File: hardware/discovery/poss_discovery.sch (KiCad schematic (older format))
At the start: 28 parts, among them SW1 SW_PUSH, SW10 SW_PUSH, SW11 SW_PUSH, SW12 SW_PUSH, SW13 SW_PUSH, SW14 SW_PUSH, SW15 SW_PUSH, SW16 SW_PUSH, SW17 SW_PUSH, SW18 SW_PUSH, SW19 SW_PUSH, SW2 SW_PUSH, SW20 SW_PUSH, SW21 SW_PUSH, SW22 SW_PUSH, SW3 SW_PUSH, SW4 SW_PUSH, SW5 SW_PUSH, SW6 SW_PUSH, SW7 SW_PUSH, SW8 SW_PUSH, SW9 SW_PUSH, U1 STM32F4_DISCO_Header

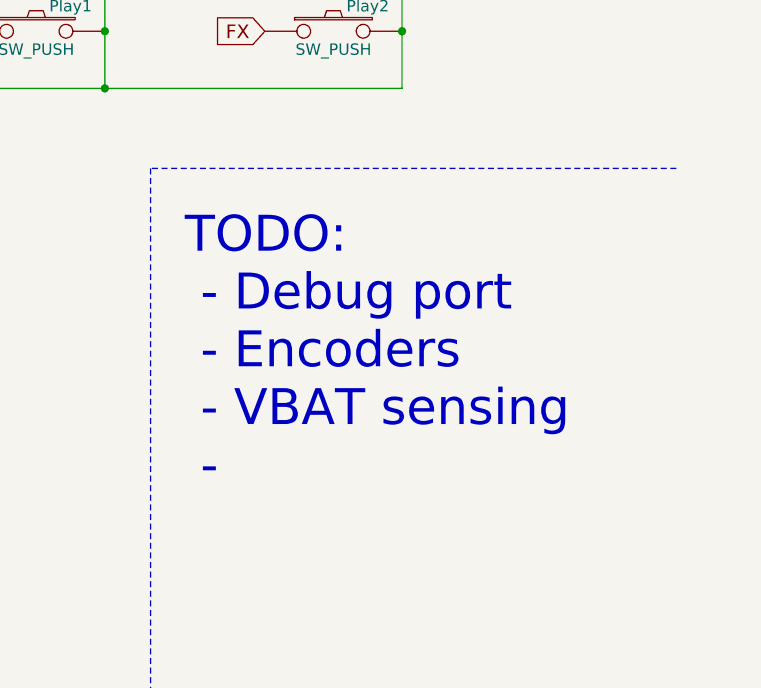
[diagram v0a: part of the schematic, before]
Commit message: Discovery: add crystal
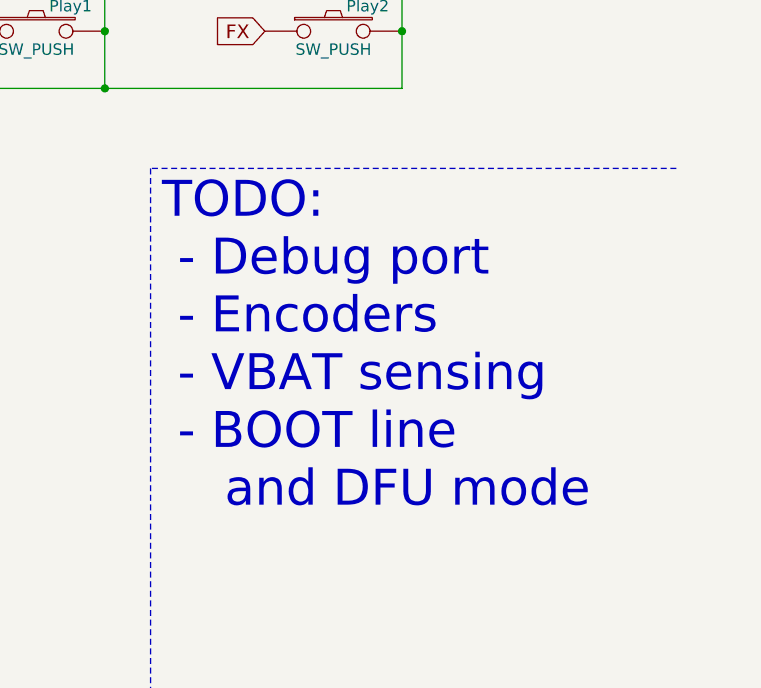
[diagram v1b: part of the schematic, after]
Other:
- note added: "TODO:\n - Debug port\n - Encoders\n - VBAT sensing\n - BOOT line \n and DFU mode"
- note removed: "TODO:\n - Debug port\n - Encoders\n - VBAT sensing\n -"
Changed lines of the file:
@@
 F1 "audio.sch" 60
 $EndSheet
-Text Notes 9000 5500 0    157  ~ 0
-TODO:\n - Debug port\n - Encoders\n - VBAT sensing\n -
+Text Notes 8900 5600 0    157  ~ 0
+TODO:\n - Debug port\n - Encoders\n - VBAT sensing\n - BOOT line \n    and DFU mode
 Wire Wire Line
 	7400 750  7400 3750

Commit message: Discovery: STM32F4 power a filtering
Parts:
- removed RV1, RV2: POT, Potentiometers:Potentiometer_WirePads_Small, symbol POT-RESCUE-poss_discovery
- added U6, U7: encoder_and_switch, symbol encoder_and_switch
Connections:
- net labels added: ENC_1_A, ENC_1_B, ENC_1_SW, ENC_2_A, ENC_2_B, ENC_2_SW
- wire segments 14 -> 6
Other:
- note added: "TODO:\n - Debug port\n - Encoders\n - VBAT sensing\n - BOOT line \n and DFU mode\n - NReset pull-up"
- note removed: "TODO:\n - Debug port\n - Encoders\n - VBAT sensing\n - BOOT line \n and DFU mode"
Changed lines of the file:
@@
-$EndComp
-$Comp
-L POT-RESCUE-poss_discovery RV2
-U 1 1 583F8AB3
-P 4700 5900
-F 0 "RV2" H 4700 5820 50  0000 C CNN
-F 1 "POT" H 4700 5900 50  0000 C CNN
-F 2 "Potentiometers:Potentiometer_WirePads_Small" H 4700 5900 50  0001 C CNN
-F 3 "" H 4700 5900 50  0000 C CNN
-	1    4700 5900
-	1    0    0    -1
-$EndComp
-$Comp
-L POT-RESCUE-poss_discovery RV1
-U 1 1 583FAB8F
-P 3350 5900
-F 0 "RV1" H 3350 5820 50  0000 C CNN
-F 1 "POT" H 3350 5900 50  0000 C CNN
-F 2 "Potentiometers:Potentiometer_WirePads_Small" H 3350 5900 50  0001 C CNN
-F 3 "" H 3350 5900 50  0000 C CNN
-	1    3350 5900
-	1    0    0    -1
 $EndComp
 $Comp
@@
 Text GLabel 4400 1650 0    60   Input ~ 0
 3V3
-Text GLabel 3350 5650 2    60   Input ~ 0
-POT1
-Text GLabel 4700 5650 2    60   Input ~ 0
-POT2
-Text GLabel 3100 5900 0    60   Input ~ 0
-3V3
-Text GLabel 4450 5900 0    60   Input ~ 0
-3V3
 Text GLabel 2200 1350 2    60   Input ~ 0
 GND
@@
 F1 "power.sch" 60
 $EndSheet
+Text GLabel 5500 4950 2    60   Input ~ 0
+GND
 $Comp
 L GND #PWR01
-U 1 1 585DAFE1
-P 4950 6000
-F 0 "#PWR01" H 4950 6000 30  0001 C CNN
-F 1 "GND" H 4950 5930 30  0001 C CNN
-F 2 "" H 4950 6000 60  0001 C CNN
-F 3 "" H 4950 6000 60  0001 C CNN
-	1    4950 6000
-	1    0    0    -1
-$EndComp
-$Comp
-L GND #PWR02
-U 1 1 585DB05F
-P 3600 6000
-F 0 "#PWR02" H 3600 6000 30  0001 C CNN
-F 1 "GND" H 3600 5930 30  0001 C CNN
-F 2 "" H 3600 6000 60  0001 C CNN
-F 3 "" H 3600 6000 60  0001 C CNN
-	1    3600 6000
-	1    0    0    -1
-$EndComp
-Text GLabel 5500 4950 2    60   Input ~ 0
-GND
-$Comp
-L GND #PWR03
 U 1 1 585DBA46
 P 5500 5100
-F 0 "#PWR03" H 5500 5100 30  0001 C CNN
+F 0 "#PWR01" H 5500 5100 30  0001 C CNN
 F 1 "GND" H 5500 5030 30  0001 C CNN
 F 2 "" H 5500 5100 60  0001 C CNN
@@
 F1 "audio.sch" 60
 $EndSheet
-Text Notes 8900 5600 0    157  ~ 0
-TODO:\n - Debug port\n - Encoders\n - VBAT sensing\n - BOOT line \n    and DFU mode
+Text Notes 8950 5850 0    157  ~ 0
+TODO:\n - Debug port\n - Encoders\n - VBAT sensing\n - BOOT line \n    and DFU mode\n - NReset pull-up
 Wire Wire Line
 	7400 750  7400 3750
@@
 Connection ~ 9950 1800
 Connection ~ 9950 1450
-Wire Wire Line
-	4850 5900 4950 5900
-Wire Wire Line
-	4700 5750 4700 5650
-Wire Wire Line
-	4550 5900 4450 5900
-Wire Wire Line
-	3500 5900 3600 5900
-Wire Wire Line
-	3350 5750 3350 5650
-Wire Wire Line
-	3200 5900 3100 5900
 Connection ~ 9950 3500
 Connection ~ 8650 3500
 Connection ~ 7400 3500
-Wire Wire Line
-	3600 5900 3600 6000
-Wire Wire Line
-	4950 5900 4950 6000
 Wire Wire Line
 	5350 4950 5500 4950
@@
 Text GLabel 6800 3750 0    60   Input ~ 0
 WAKEUP
+$Comp
+L encoder_and_switch U6
+U 1 1 585F9C7A
+P 1750 5250
+F 0 "U6" H 1500 5050 60  0000 C CNN
+F 1 "encoder_and_switch" H 2100 5100 60  0000 C CNN
+F 2 "" H 1750 5250 60  0001 C CNN
+F 3 "" H 1750 5250 60  0001 C CNN
+	1    1750 5250
+	1    0    0    -1
+$EndComp
+$Comp
+L encoder_and_switch U7
+U 1 1 585FA833
+P 3750 5250
+F 0 "U7" H 3500 5050 60  0000 C CNN
+F 1 "encoder_and_switch" H 4100 5100 60  0000 C CNN
+F 2 "" H 3750 5250 60  0001 C CNN
+F 3 "" H 3750 5250 60  0001 C CNN
+	1    3750 5250
+	1    0    0    -1
+$EndComp
+Text GLabel 2150 5600 2    60   Input ~ 0
+WAKEUP
+Text GLabel 4150 5600 2    60   Input ~ 0
+WAKEUP
+Text GLabel 1350 5600 0    60   Input ~ 0
+ENC_1_SW
+Text GLabel 3350 5600 0    60   Input ~ 0
+ENC_2_SW
+Text GLabel 1500 5950 3    60   Input ~ 0
+ENC_1_A
+Text GLabel 1750 5950 3    60   Input ~ 0
+WAKEUP
+Text GLabel 2000 5950 3    60   Input ~ 0
+ENC_1_B
+Text GLabel 3500 5950 3    60   Input ~ 0
+ENC_2_A
+Text GLabel 3750 5950 3    60   Input ~ 0
+WAKEUP
+Text GLabel 4000 5950 3    60   Input ~ 0
+ENC_2_B
 $EndSCHEMATC

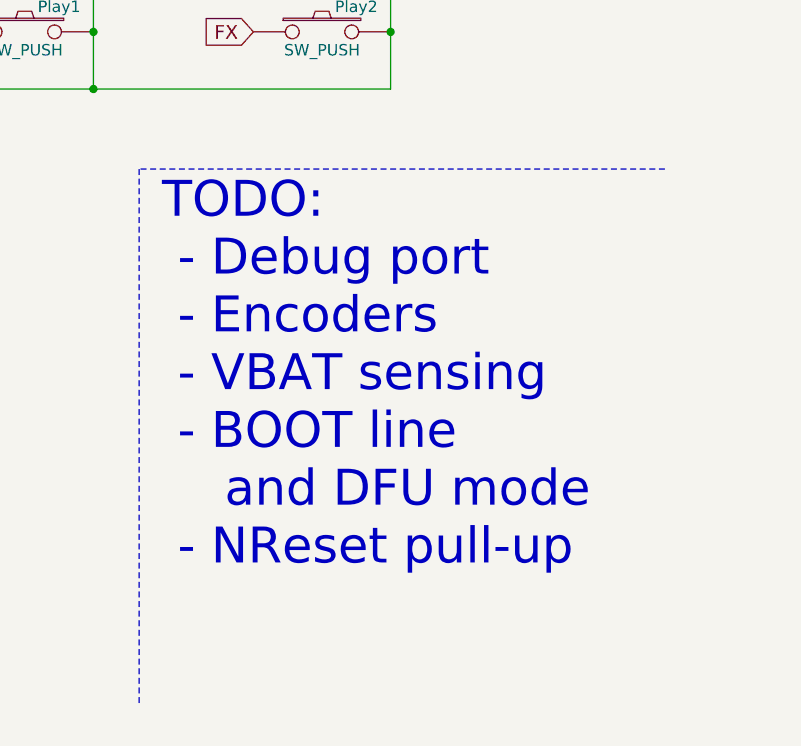
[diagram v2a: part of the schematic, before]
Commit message: Discovery: Start routing LEDs and buttons
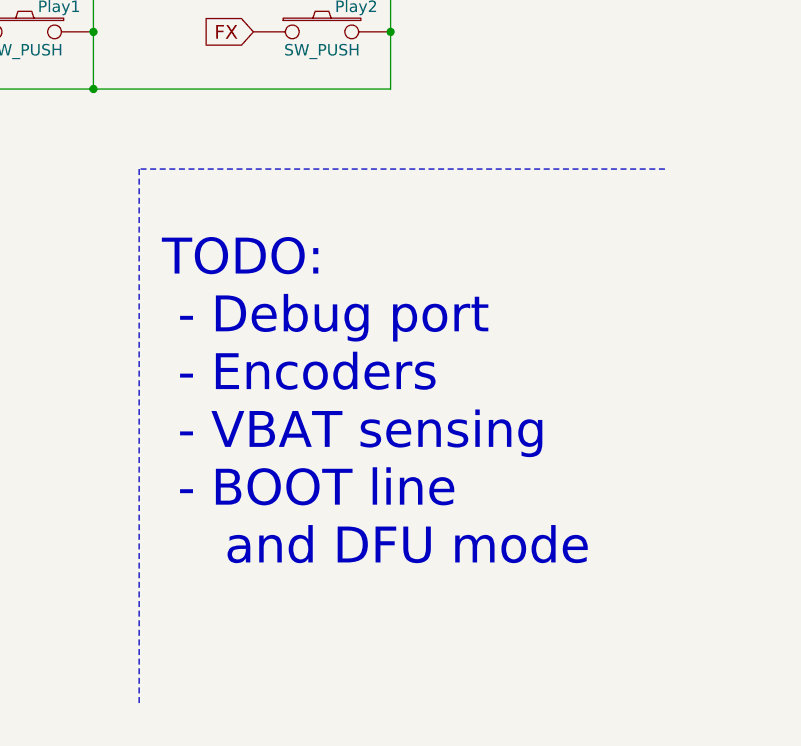
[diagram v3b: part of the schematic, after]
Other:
- note added: "TODO:\n - Debug port\n - Encoders\n - VBAT sensing\n - BOOT line \n and DFU mode"
- note removed: "TODO:\n - Debug port\n - Encoders\n - VBAT sensing\n - BOOT line \n and DFU mode\n - NReset pull-up"
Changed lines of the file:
@@
 $EndSheet
 Text Notes 8950 5850 0    157  ~ 0
-TODO:\n - Debug port\n - Encoders\n - VBAT sensing\n - BOOT line \n    and DFU mode\n - NReset pull-up
+TODO:\n - Debug port\n - Encoders\n - VBAT sensing\n - BOOT line \n    and DFU mode
 Wire Wire Line
 	7400 750  7400 3750

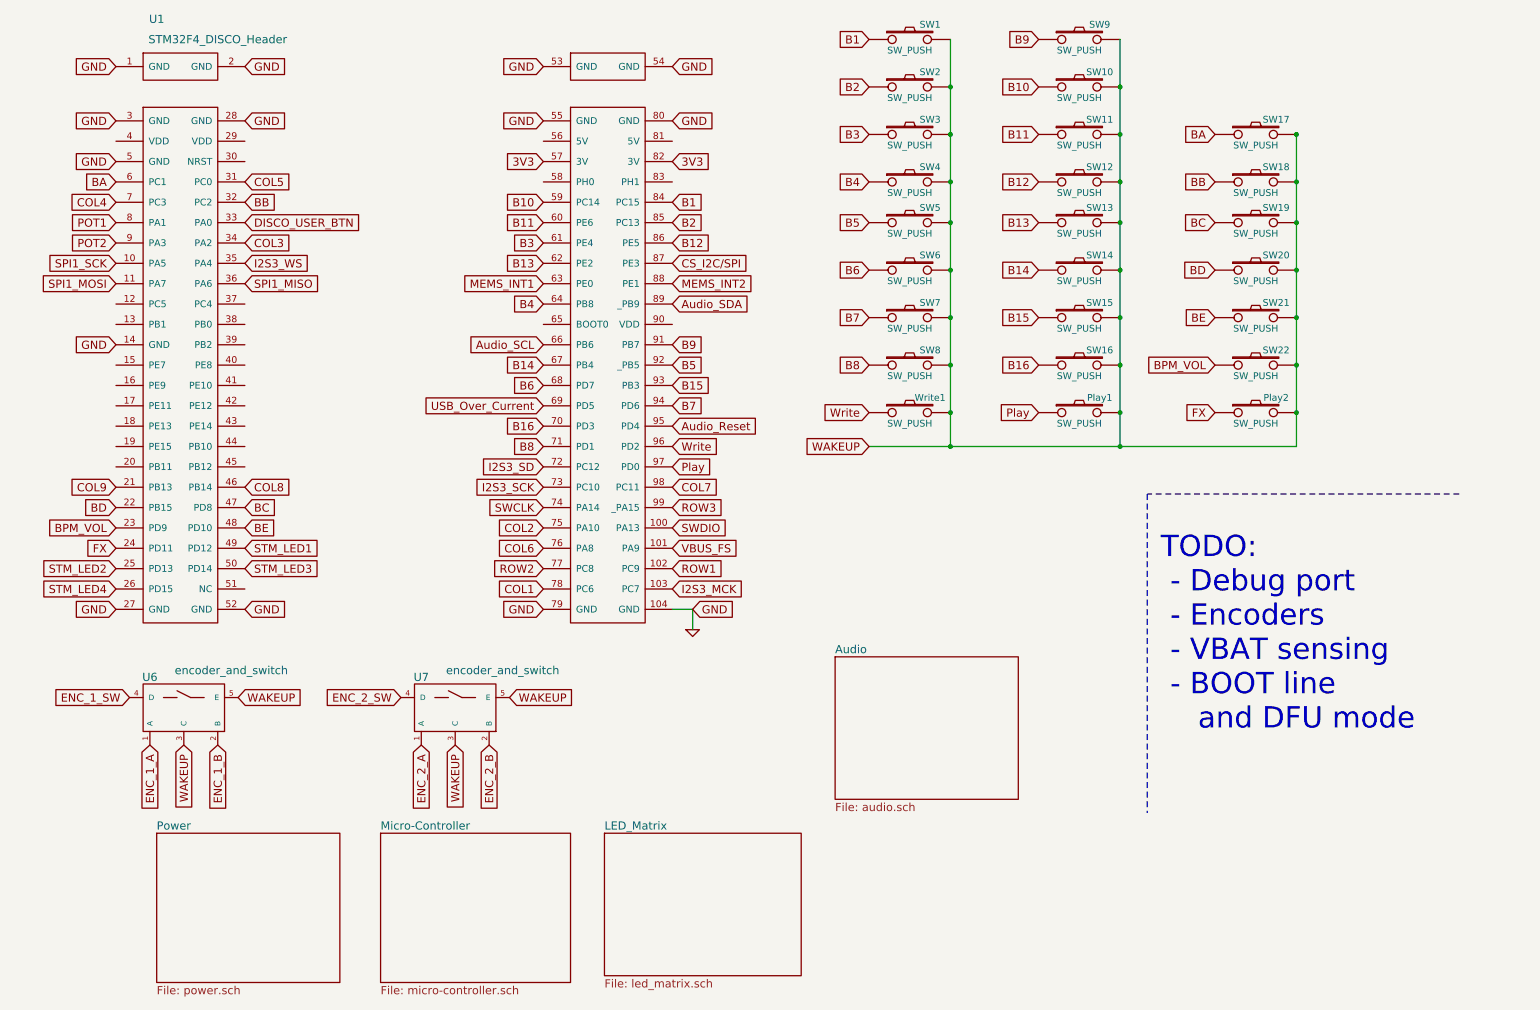
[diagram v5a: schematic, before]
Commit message: Discovery: Add two encoders and remove the BPM button
BPM and volume will be changed with a long press of the play button and
the encoders
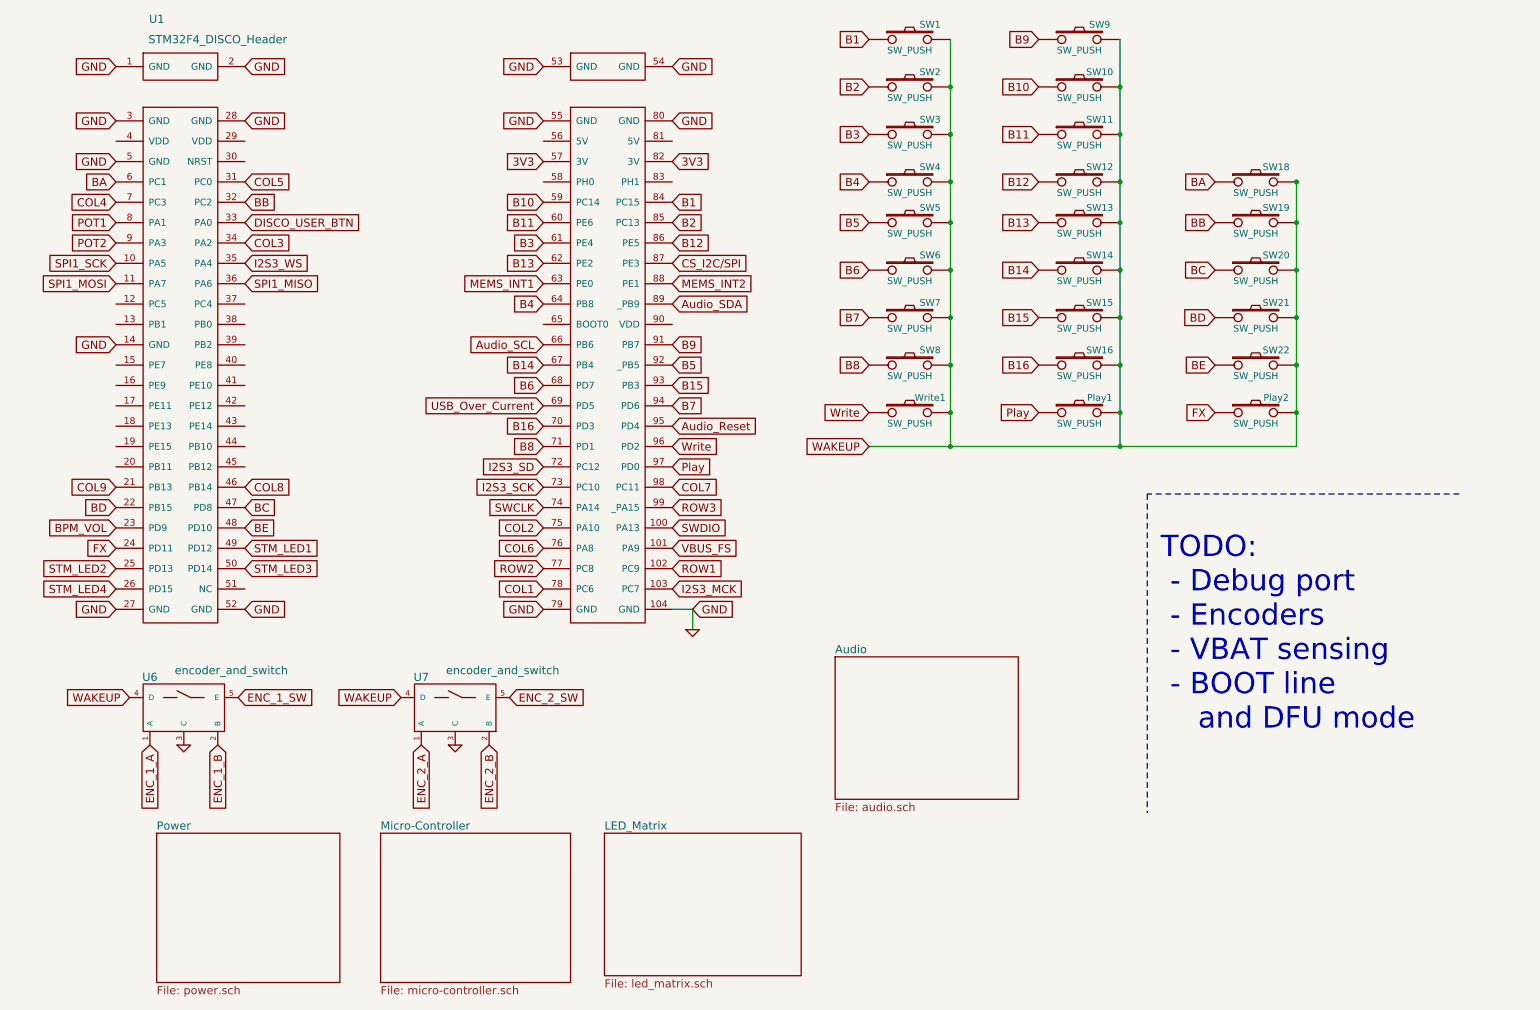
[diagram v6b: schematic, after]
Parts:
- removed SW17: SW_PUSH, Buttons_Switches_SMD:SW_SPST_B3SL-1002P, symbol SW_PUSH
- U6, U7: footprint (none) -> stm32f4-disco:encoder_EC12D
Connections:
- net BA: now also SW18.1
- net BB: now also SW19.1; no longer SW18.1
- net BC: now also SW20.1; no longer SW19.1
- net BD: now also SW21.1; no longer SW20.1
- net BE: now also SW22.1; no longer SW21.1
- net BPM_VOL: no longer SW22.1
- net ENC_1_SW: now also U6.5 (E); no longer U6.4 (D)
- net ENC_2_SW: now also U7.5 (E); no longer U7.4 (D)
- net GND: now also U6.3 (C), U7.3 (C)
- net WAKEUP: now also U6.4 (D), U7.4 (D); no longer U6.3 (C), U6.5 (E), U7.3 (C), U7.5 (E)
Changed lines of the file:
@@
-$EndComp
-$Comp
-L SW_PUSH SW17
-U 1 1 583EF8EE
-P 9650 1450
-F 0 "SW17" H 9800 1560 50  0000 C CNN
-F 1 "SW_PUSH" H 9650 1370 50  0000 C CNN
-F 2 "Buttons_Switches_SMD:SW_SPST_B3SL-1002P" H 9650 1450 50  0001 C CNN
-F 3 "" H 9650 1450 50  0000 C CNN
-	1    9650 1450
-	1    0    0    -1
 $EndComp
 $Comp
@@
 Text GLabel 2200 950  2    60   Input ~ 0
 GND
-Text GLabel 9350 1450 0    60   Input ~ 0
+Text GLabel 9350 1800 0    60   Input ~ 0
 BA
-Text GLabel 9350 1800 0    60   Input ~ 0
+Text GLabel 9350 2100 0    60   Input ~ 0
 BB
-Text GLabel 9350 2100 0    60   Input ~ 0
+Text GLabel 9350 2450 0    60   Input ~ 0
 BC
-Text GLabel 9350 2450 0    60   Input ~ 0
+Text GLabel 9350 2800 0    60   Input ~ 0
 BD
-Text GLabel 9350 2800 0    60   Input ~ 0
+Text GLabel 9350 3150 0    60   Input ~ 0
 BE
-Text GLabel 9350 3150 0    60   Input ~ 0
-BPM_VOL
 Text GLabel 9350 3500 0    60   Input ~ 0
 FX
@@
 Text Notes 8950 5850 0    157  ~ 0
 TODO:\n - Debug port\n - Encoders\n - VBAT sensing\n - BOOT line \n    and DFU mode
+Text GLabel 6800 3750 0    60   Input ~ 0
+WAKEUP
+$Comp
+L encoder_and_switch U6
+U 1 1 585F9C7A
+P 1750 5250
+F 0 "U6" H 1500 5050 60  0000 C CNN
+F 1 "encoder_and_switch" H 2100 5100 60  0000 C CNN
+F 2 "stm32f4-disco:encoder_EC12D" H 1750 5250 60  0001 C CNN
+F 3 "" H 1750 5250 60  0001 C CNN
+	1    1750 5250
+	1    0    0    -1
+$EndComp
+$Comp
+L encoder_and_switch U7
+U 1 1 585FA833
+P 3750 5250
+F 0 "U7" H 3500 5050 60  0000 C CNN
+F 1 "encoder_and_switch" H 4100 5100 60  0000 C CNN
+F 2 "stm32f4-disco:encoder_EC12D" H 3750 5250 60  0001 C CNN
+F 3 "" H 3750 5250 60  0001 C CNN
+	1    3750 5250
+	1    0    0    -1
+$EndComp
+Text GLabel 1350 5600 0    60   Input ~ 0
+WAKEUP
+Text GLabel 3350 5600 0    60   Input ~ 0
+WAKEUP
+Text GLabel 2150 5600 2    60   Input ~ 0
+ENC_1_SW
+Text GLabel 4150 5600 2    60   Input ~ 0
+ENC_2_SW
+Text GLabel 1500 5950 3    60   Input ~ 0
+ENC_1_A
+Text GLabel 2000 5950 3    60   Input ~ 0
+ENC_1_B
+Text GLabel 3500 5950 3    60   Input ~ 0
+ENC_2_A
+Text GLabel 4000 5950 3    60   Input ~ 0
+ENC_2_B
+$Comp
+L GND #PWR02
+U 1 1 586532D8
+P 3750 5950
+F 0 "#PWR02" H 3750 5950 30  0001 C CNN
+F 1 "GND" H 3750 5880 30  0001 C CNN
+F 2 "" H 3750 5950 60  0001 C CNN
+F 3 "" H 3750 5950 60  0001 C CNN
+	1    3750 5950
+	1    0    0    -1
+$EndComp
+$Comp
+L GND #PWR03
+U 1 1 58653337
+P 1750 5950
+F 0 "#PWR03" H 1750 5950 30  0001 C CNN
+F 1 "GND" H 1750 5880 30  0001 C CNN
+F 2 "" H 1750 5950 60  0001 C CNN
+F 3 "" H 1750 5950 60  0001 C CNN
+	1    1750 5950
+	1    0    0    -1
+$EndComp
 Wire Wire Line
 	7400 750  7400 3750
@@
 Connection ~ 8650 1450
 Connection ~ 8650 1100
-Wire Wire Line
-	9950 3750 9950 1450
 Connection ~ 9950 3150
 Connection ~ 9950 2800
@@
 Connection ~ 9950 2100
 Connection ~ 9950 1800
-Connection ~ 9950 1450
 Connection ~ 9950 3500
 Connection ~ 8650 3500
@@
 	8850 4100 8850 6450
 Wire Wire Line
-	6800 3750 9950 3750
+	9950 3750 6800 3750
 Connection ~ 8650 3750
 Connection ~ 7400 3750
-Text GLabel 6800 3750 0    60   Input ~ 0
-WAKEUP
-$Comp
-L encoder_and_switch U6
-U 1 1 585F9C7A
-P 1750 5250
-F 0 "U6" H 1500 5050 60  0000 C CNN
-F 1 "encoder_and_switch" H 2100 5100 60  0000 C CNN
-F 2 "" H 1750 5250 60  0001 C CNN
-F 3 "" H 1750 5250 60  0001 C CNN
-	1    1750 5250
-	1    0    0    -1
-$EndComp
-$Comp
-L encoder_and_switch U7
-U 1 1 585FA833
-P 3750 5250
-F 0 "U7" H 3500 5050 60  0000 C CNN
-F 1 "encoder_and_switch" H 4100 5100 60  0000 C CNN
-F 2 "" H 3750 5250 60  0001 C CNN
-F 3 "" H 3750 5250 60  0001 C CNN
-	1    3750 5250
-	1    0    0    -1
-$EndComp
-Text GLabel 2150 5600 2    60   Input ~ 0
-WAKEUP
-Text GLabel 4150 5600 2    60   Input ~ 0
-WAKEUP
-Text GLabel 1350 5600 0    60   Input ~ 0
-ENC_1_SW
-Text GLabel 3350 5600 0    60   Input ~ 0
-ENC_2_SW
-Text GLabel 1500 5950 3    60   Input ~ 0
-ENC_1_A
-Text GLabel 1750 5950 3    60   Input ~ 0
-WAKEUP
-Text GLabel 2000 5950 3    60   Input ~ 0
-ENC_1_B
-Text GLabel 3500 5950 3    60   Input ~ 0
-ENC_2_A
-Text GLabel 3750 5950 3    60   Input ~ 0
-WAKEUP
-Text GLabel 4000 5950 3    60   Input ~ 0
-ENC_2_B
+Wire Wire Line
+	9950 1800 9950 3750
 $EndSCHEMATC
